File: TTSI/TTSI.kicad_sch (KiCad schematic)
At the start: 18 parts, among them K1 Relay_SPST-NO, Q1 NPN, U1 74AHC1G32, U2 LM555xM

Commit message: TSSI FIXES
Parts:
- removed D1: LED, symbol Device:LED
- removed D3, D5: D, symbol Device:D
- removed K1: Relay_SPST-NO, symbol Relay:Relay_SPST-NO
- removed L2: L, symbol Device:L
- removed Q1: NPN, symbol Simulation_SPICE:NPN
- removed R1, R6, R7: R_US, symbol Device:R_US
- added D101: D, symbol Device:D
- added Q101, Q102: PMOS, symbol Simulation_SPICE:PMOS
- added R103, R104: ?, symbol Device:R_US
- added R106: R_US, symbol Device:R_US
- added U103: 74AHC1G08, symbol 74xGxx:74AHC1G08
- C101: renamed from C2; value C -> .01u
- R101: renamed from R3; value R_US -> 10k
- R102: renamed from R2; value R_US -> 2.2k
- R105: renamed from R5; value R_US -> 100k
- renumbered C1 to C102, D2 to D104, R4 to R107, U1 to U101, U2 to U102
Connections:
- net +12V: now also R101.1
- net +5V: now also R105.2, U102.4 (R), U102.8 (VCC), Q101.3 (S), Q102.3 (S), U103.5 (VCC)
- net GND: now also C101.2, D101.1 (K), R104.2, U103.3 (GND); no longer R101.1
- net IMD: no longer U101.2
- net THRESH: now reaches C102.2, U102.2 (TR)
- net THRESH: now also R105.1, U102.6 (THR), R106.2
- net at D104.2 (A): now also U103.4; no longer U102.3 (Q)
- net at U102.7 (DIS): no longer R105.1
- net at U101.4: now also Q101.2 (G)
- net BSE: no longer names the net of U101.1
- net BSE: no longer R101.2
- new net: Q102.1 (D), R104.1, U103.2
- new net: Q101.1 (D), Q102.2 (G), R103.1
- new net: D101.2 (A), R103.2
- new net BMS: R101.2
- new net OUT: R106.1, U102.3 (Q), U103.1
- no-connect marks 0 -> 1
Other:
- note added: "LEVEL SHIFT"
- note added: "f = 1 / (0.693 * (2R106) * C102)"
- note added: "https://www.electronics-tutorials.ws/waveforms/555_oscillator.html"
- note removed: "FEED BACK DIODE"
- note removed: "Green LED"
- company: (none) -> FSAE
- title: (none) -> TSSI
- moved on the sheet: C101, C102, D104, R101, R102, R105, R107, U101, U102

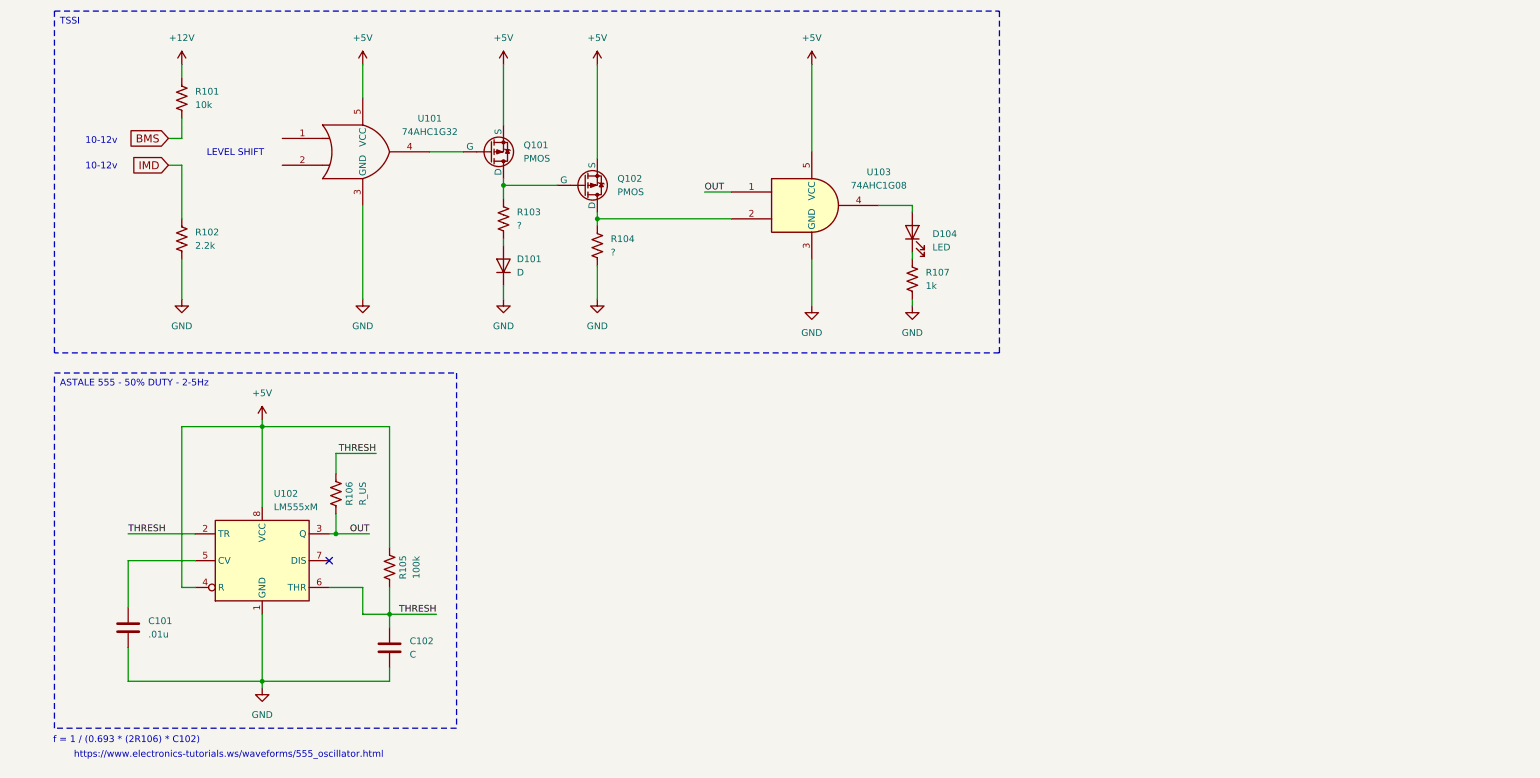
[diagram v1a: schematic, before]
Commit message: Improved TSSI
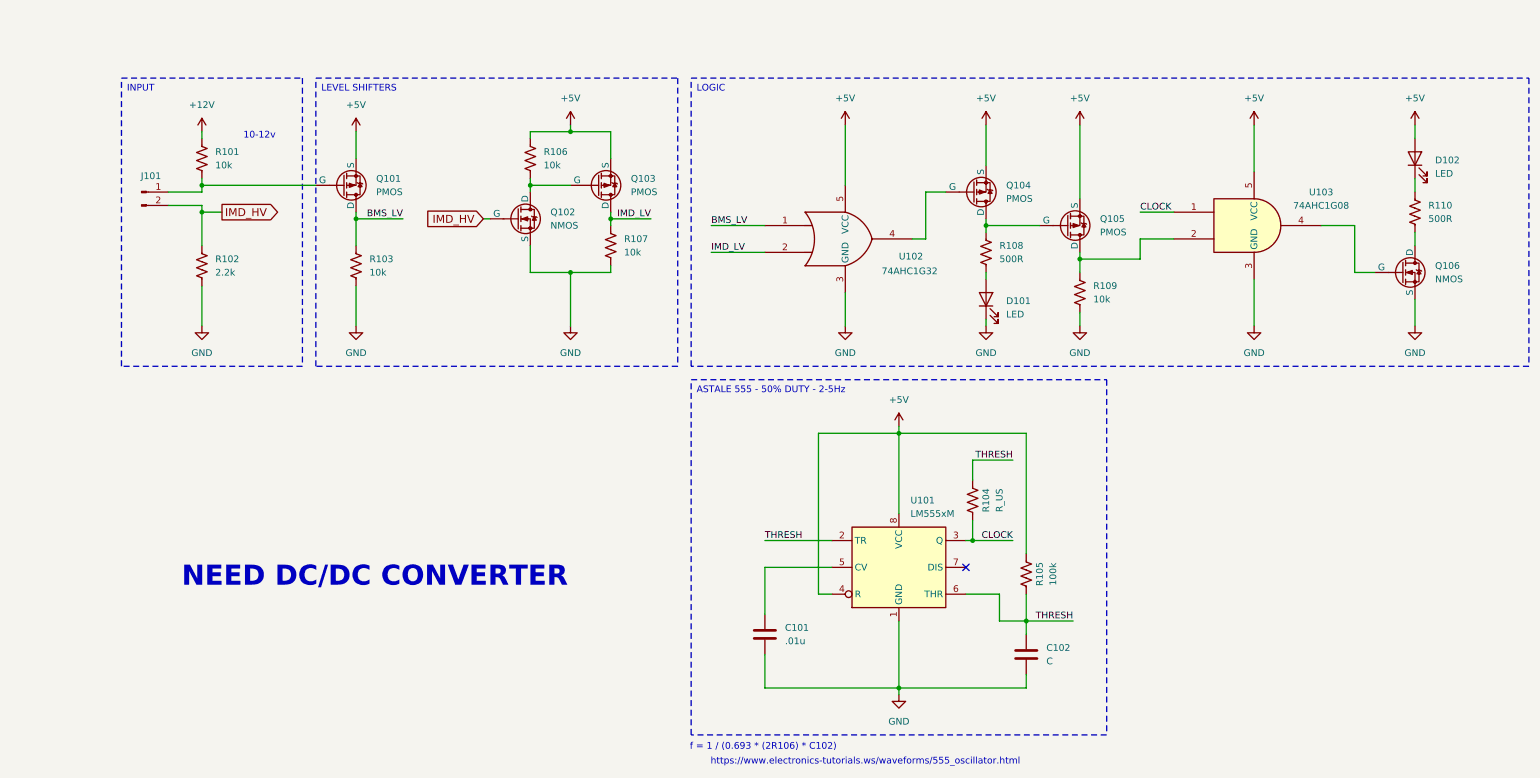
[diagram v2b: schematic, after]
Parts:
- removed D101: D, symbol Device:D
- added D101: LED, symbol Device:LED
- added J101: Conn_01x02_Pin, symbol Connector:Conn_01x02_Pin
- added Q101, Q103: PMOS, symbol Simulation_SPICE:PMOS
- added Q102, Q106: NMOS, symbol Simulation_SPICE:NMOS
- added R103, R106, R107: 10k, symbol Device:R_US
- R108: renamed from R103; value ? -> 500R
- R109: renamed from R104; value ? -> 10k
- R110: renamed from R107; value 1k -> 500R
- renumbered D104 to D102, Q101 to Q104, Q102 to Q105, R106 to R104, U102 to U101, U101 to U102
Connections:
- net +5V: now also D102.2 (A), Q101.3 (S), Q103.3 (S), R106.1
- net GND: now also D101.1 (K), Q102.3 (S), Q106.3 (S), R103.2, R107.2; no longer R110.2
- net at U103.4: now also Q106.2 (G); no longer D102.2 (A)
- net BMS_LV: now reaches U102.1
- net BMS_LV: now also Q101.1 (D), R103.1
- net IMD_LV: now reaches U102.2
- net IMD_LV: now also Q103.1 (D), R107.1
- net at R108.2: now also D101.2 (A)
- net BMS: no longer names the net of R101.2
- net BMS: now also J101.1 (Pin_1), Q101.2 (G)
- net IMD renamed IMD_HV
- net IMD_HV: now also J101.2 (Pin_2), Q102.2 (G)
- net OUT renamed CLOCK
- new net: Q102.1 (D), Q103.2 (G), R106.2
- new net: Q106.1 (D), R110.2
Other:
- note added: "NEED DC/DC CONVERTER"
- note removed: "LEVEL SHIFT"
- moved on the sheet: C101, C102, D102, Q104, Q105, R101, R102, R104, R105, R108, R109, R110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

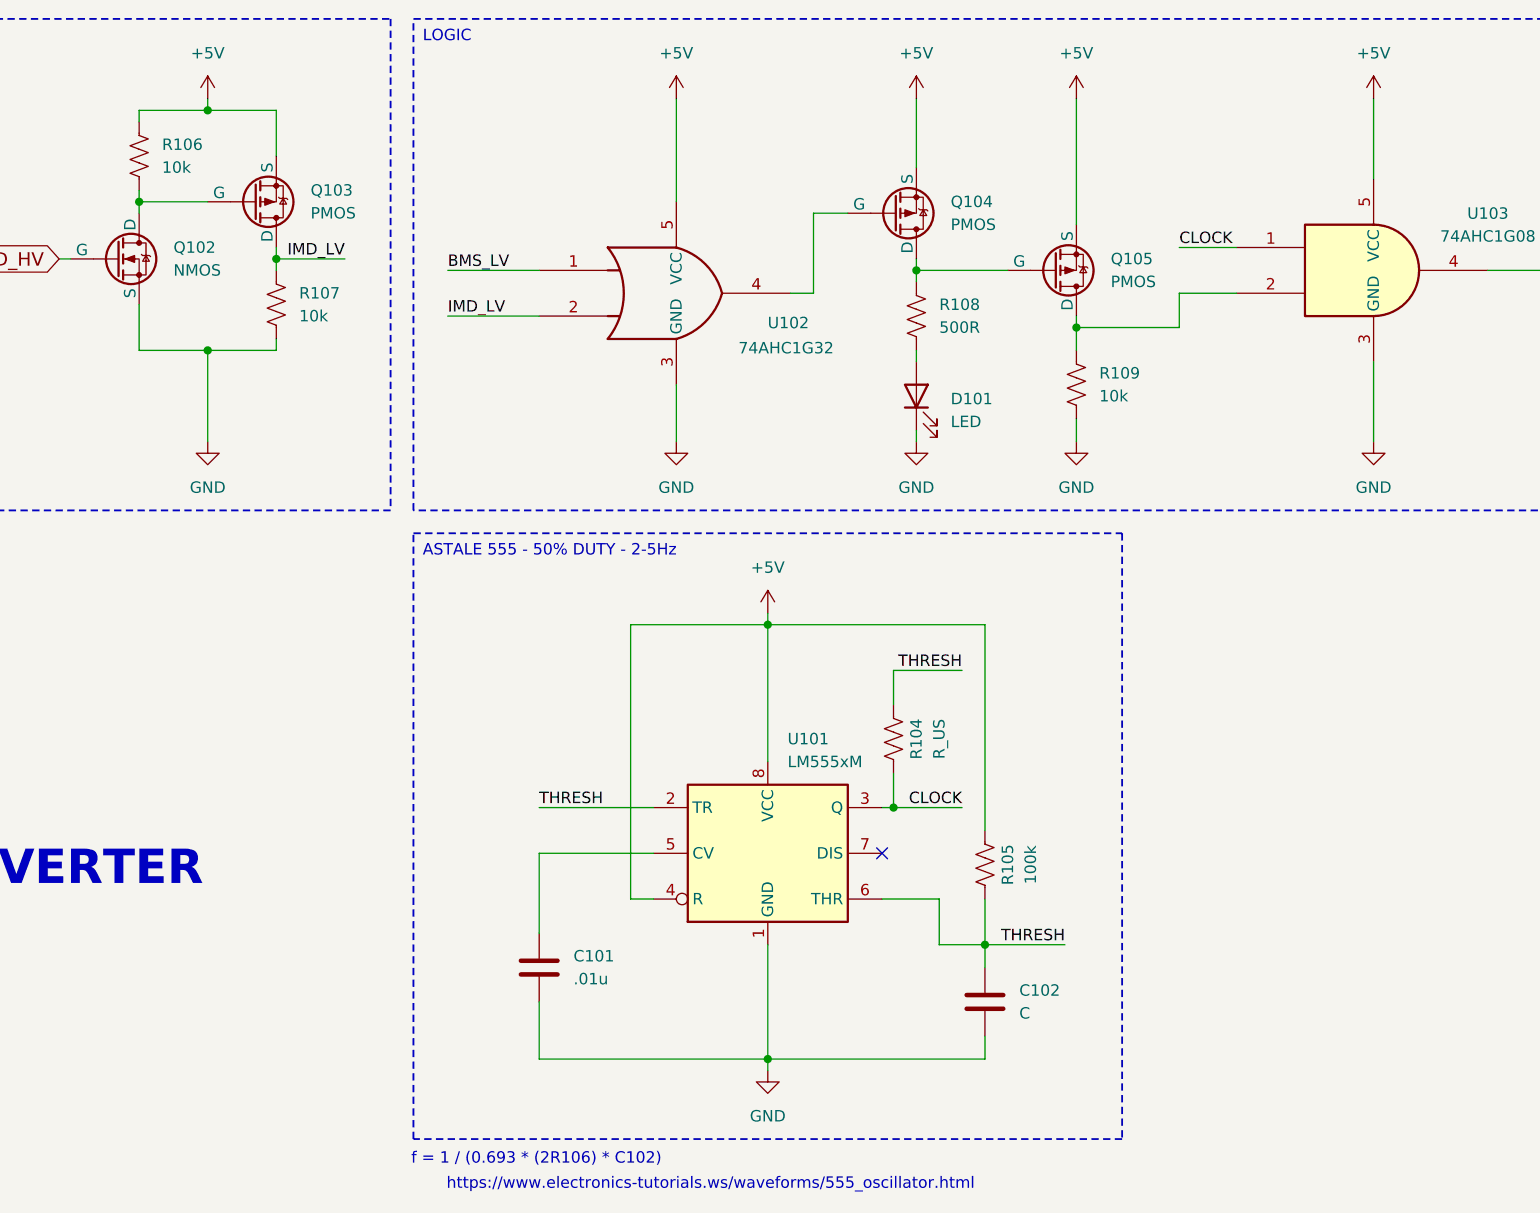
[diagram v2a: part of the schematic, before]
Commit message: TSSI BOM and BYPASS
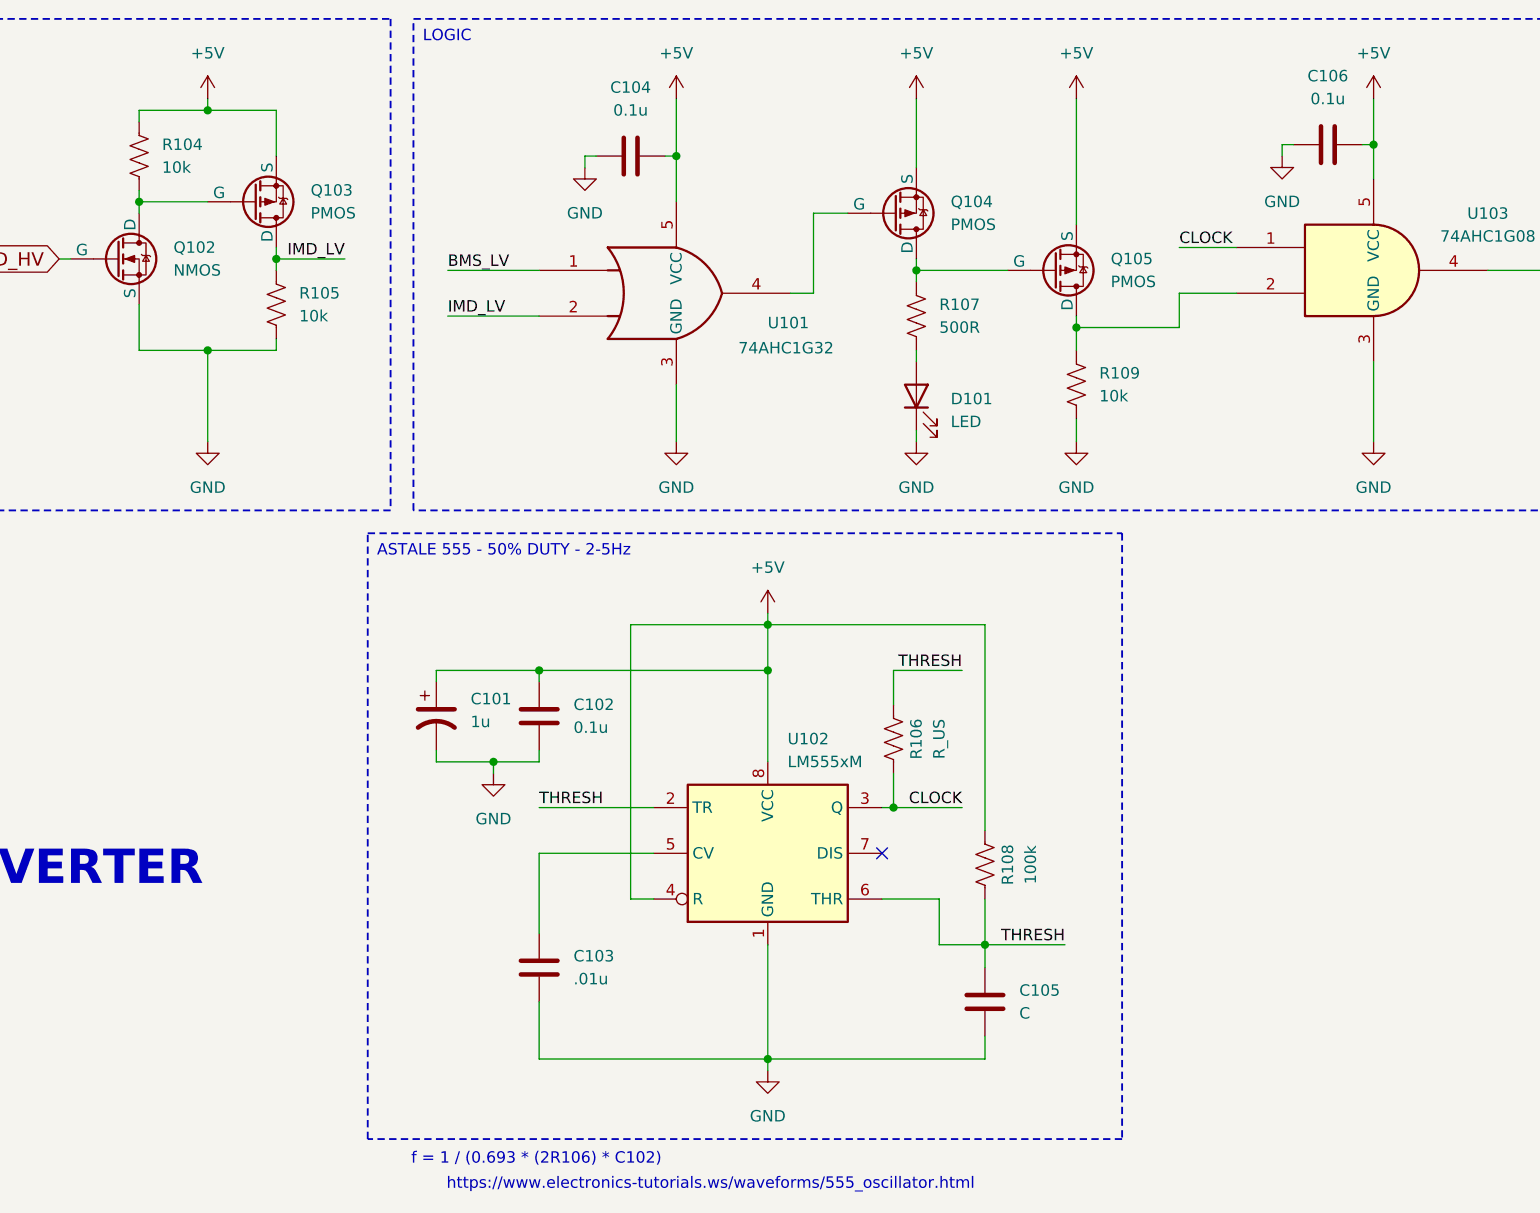
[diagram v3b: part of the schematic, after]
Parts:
- added C101: 1u, symbol Device:C_Polarized_US
- added C102, C104, C106: 0.1u, Capacitor_SMD:C_0402_1005Metric, symbol Device:C
- C103: renamed from C101; footprint (none) -> Capacitor_SMD:C_0402_1005Metric
- C105: renamed from C102; footprint (none) -> Capacitor_SMD:C_0402_1005Metric
- U101: renamed from U102; footprint Package_TO_SOT_SMD:SOT-23-5 -> Package_TO_SOT_SMD:SOT-353_SC-70-5; JLC# (none) -> C7394028
- U103: footprint (none) -> Package_TO_SOT_SMD:SOT-353_SC-70-5; JLC# (none) -> C2861162
- renumbered R106 to R104, R107 to R105, R104 to R106, R108 to R107, R105 to R108, U101 to U102
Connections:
- net +5V: now also C101.1, C102.1, C104.1, C106.1
- net GND: now also C101.2, C102.2, C104.2, C106.2

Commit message: Comments on BSPD, TSSI
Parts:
- D101: value LED -> GREEN_LED
- D102: value LED -> RED_LED
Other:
- note added: "-NEED DC/DC CONVERTER (R-78E5.0-0.5) -USE 0805 LED (SURFACE MOUNTED) -PICK CONNECTORS -spec sizes of components"
- note removed: "NEED DC/DC CONVERTER"
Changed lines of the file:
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@@
 		)
 	)
-	(text "NEED DC/DC CONVERTER"
+	(text "-NEED DC/DC CONVERTER (R-78E5.0-0.5)\n-USE 0805 LED (SURFACE MOUNTED)\n-PICK CONNECTORS\n-spec sizes of components\n"
 		(exclude_from_sim no)
-		(at 86.106 132.588 0)
+		(at 92.456 189.484 0)
 		(effects
 			(font
@@
 	(label "BMS_LV"
 		(at 91.44 64.77 180)
-		(fields_autoplaced yes)
 		(effects
 			(font
@@
 	(label "IMD_LV"
 		(at 149.86 71.12 0)
-		(fields_autoplaced yes)
 		(effects
 			(font
@@
 	(label "IMD_LV"
 		(at 138.43 64.77 180)
-		(fields_autoplaced yes)
 		(effects
 			(font
@@
 	(label "BMS_LV"
 		(at 149.86 66.04 0)
-		(fields_autoplaced yes)
 		(effects
 			(font
@@
 	(label "CLOCK"
 		(at 231.14 63.5 0)
-		(fields_autoplaced yes)
 		(effects
 			(font
@@
 	(label "THRESH"
 		(at 207.01 110.49 180)
-		(fields_autoplaced yes)
 		(effects
 			(font
@@
 	(label "THRESH"
 		(at 160.02 125.73 0)
-		(fields_autoplaced yes)
 		(effects
 			(font
@@
 	(label "THRESH"
 		(at 218.44 140.97 180)
-		(fields_autoplaced yes)
 		(effects
 			(font
@@
 	(label "CLOCK"
 		(at 207.01 125.73 180)
-		(fields_autoplaced yes)
 		(effects
 			(font
@@
 			)
 		)
-		(property "Value" "LED"
+		(property "Value" "GREEN_LED"
 			(at 205.74 82.8674 90)
 			(effects
@@
 			)
 		)
-		(property "Value" "LED"
+		(property "Value" "RED_LED"
 			(at 287.02 56.1974 90)
 			(effects
